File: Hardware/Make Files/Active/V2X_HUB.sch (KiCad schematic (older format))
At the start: 3 parts

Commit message: Saving V1.1 as archive.
We are trying a new architecture where the FTDI can be removed. making a
backup spot
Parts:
- removed F?: 1A, Resistors_SMD:R_1210, symbol FUSE
- removed P?: USB_A, Connect:USB_A, symbol USB_A
- removed P?: USB_u, Connect:USB_Micro-B, symbol USB_OTG
- added C58, C61: 1U, symbol C
- added C59, C60: 100N, symbol C
- added C62, C63: 18P, symbol C
- added R73, R77: DNS, symbol R
- added R74, R76, R78, R79: 1K0, symbol R
- added R75: 12K, symbol R
- added U18: USB2242, symbol USB2242
- added Y1: 24MHz, symbol Crystal_Small
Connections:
- net labels added: 3V3_B, FTDI_DM, FTDI_DP, HUB_CLK, HUB_CLKN, HUB_DM, HUB_DP, HUB_PWR_PRT1, HUB_PWR_PRT2, HUB_SCL, HUB_SDA, HUB_STATUS, HUB_SUSP, HUB_SUSP_IND, SIM_DM, SIM_DP, ~HUB_RESET
- net labels removed: 5V0, 5V0_OUT, USB_M, USB_P
- wire segments 3 -> 27
- no-connect marks 2 -> 3
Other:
- note added: "Boot Strapping Option\nPRTPWR1 = Battery Charge Enable\n0 = feature off, we dont need."
- note added: "Boot Strapping Option\nSUSP_IND = NON_REM0\nSMBDATA = NON_REM1\nNON_REM[1:0] = 10 \nmeans neither down port\n is removable \n\n\nSMBCLK = CFG_SEL = '0'\nMeans the hub is self powered"
- note added: "PRTPWR1 and PRTPWR2 go\n high when the port is active"
- note removed: "HOST Data/Power Connection"
- note removed: "HOST Power Connection"

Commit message: V1.2 mostly done
BOM is integrated and creates mouser orders
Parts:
- removed C58: 1U, symbol C
- removed C62, C63: 18P, symbol C
- removed R74, R76: 1K0, symbol R
- removed Y1: 24MHz, symbol Crystal_Small
- added C61: 100N, Capacitors_SMD:C_0603, symbol C
- added R80, R82: 1K0, symbol R
- added X?: 24MHz, symbol CRYSTAL_SMD
- C59: value 100N -> 1U; Mouse PN (none) -> 603-CC603KRX7R7BB105
- C60: footprint (none) -> Capacitors_SMD:C_0603; Mouse PN (none) -> 810-C1608X7R1E104K
- C62: renamed from C61; Mouse PN (none) -> 603-CC603KRX7R7BB105
- R78: Mouse PN (none) -> 71-CRCW0603-1.0K-E3
- R79: renamed from R75; Mouse PN (none) -> 71-CRCW0603-12K-E3
- R83: renamed from R79; Mouse PN (none) -> 71-CRCW0603-1.0K-E3
- U20: renamed from U18; Mouse PN (none) -> 579-USB2422/MJ
- renumbered R73 to R77, R77 to R81
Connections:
- net labels added: USB_INT_DM, USB_INT_DP
- net labels removed: FTDI_DM, FTDI_DP
- wire segments 27 -> 25

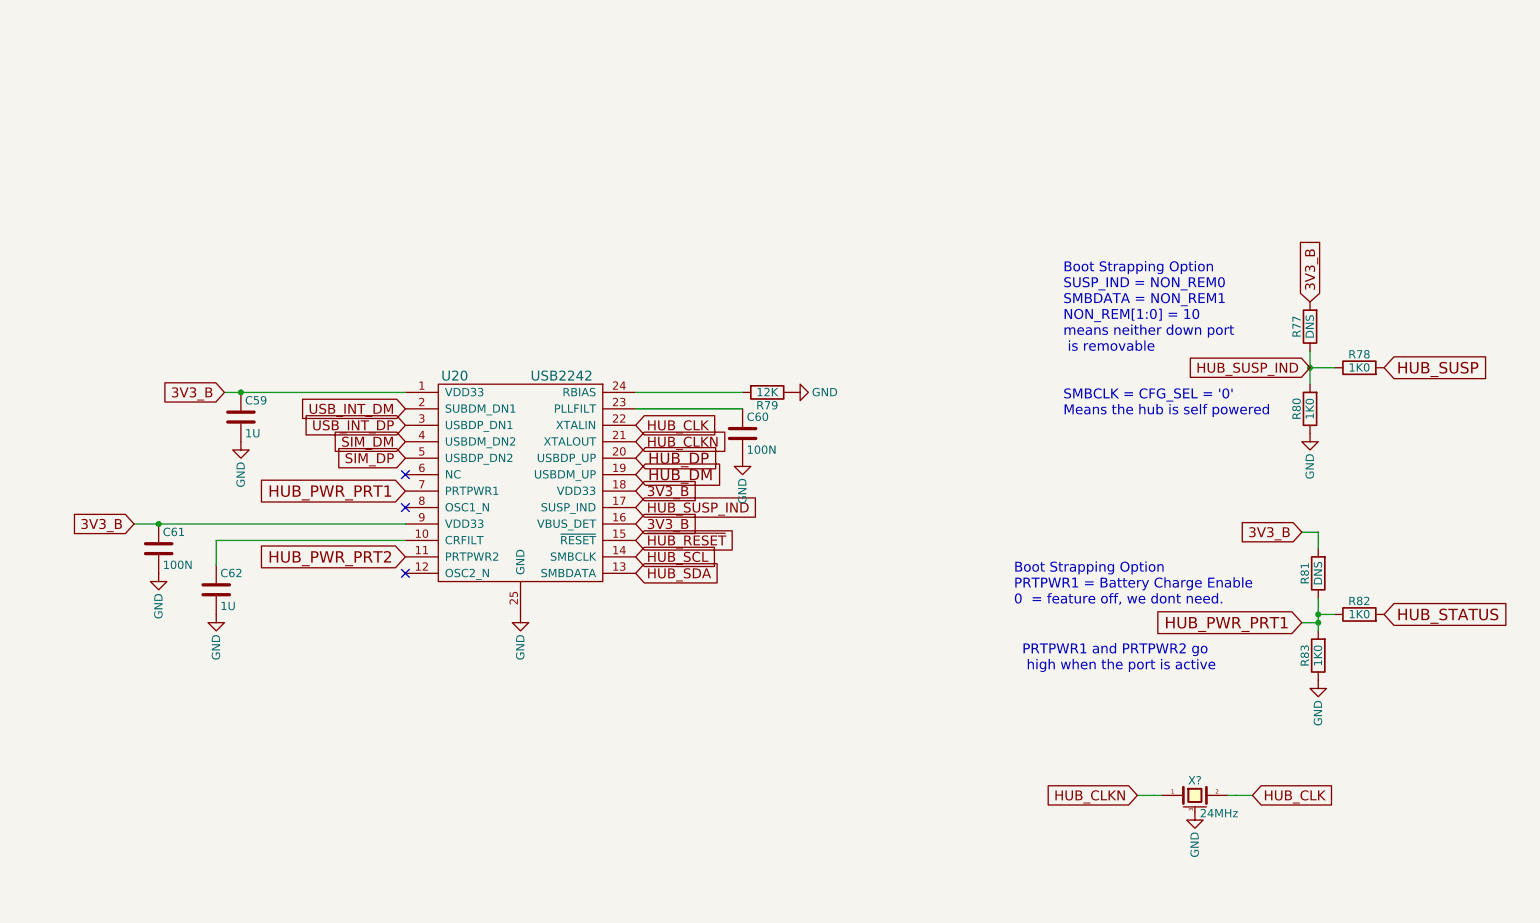
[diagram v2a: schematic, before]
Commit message: V2X v1.2 sch and bom
Made changes to the schematic to V1.2 (remove FTDI possibly) and
integrade the BOM information into the sch
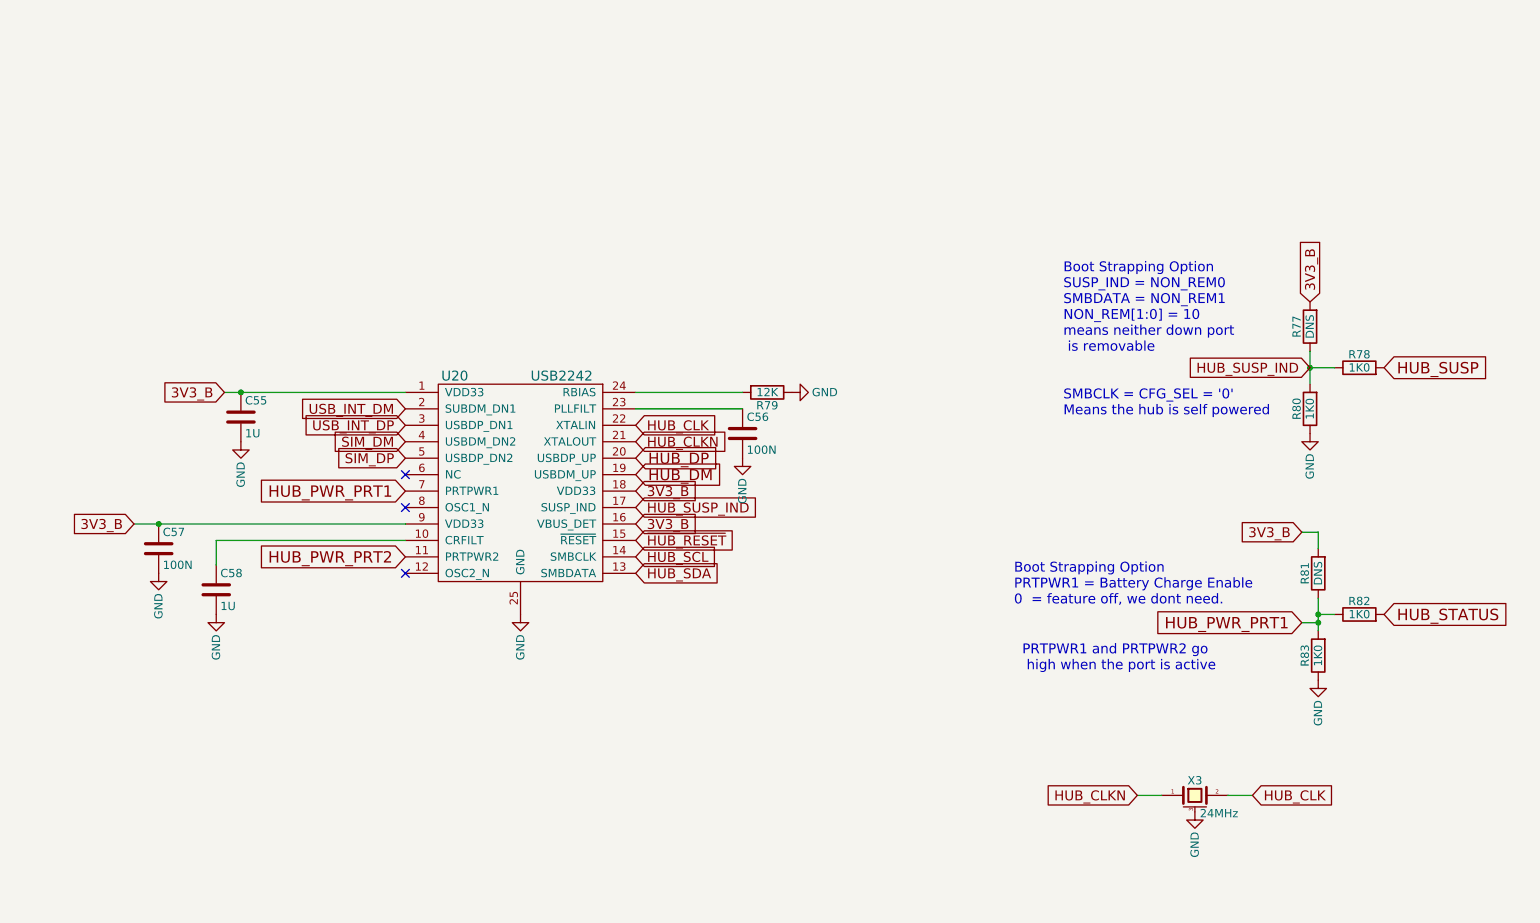
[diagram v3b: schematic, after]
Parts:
- gave numbers to parts that had none: 1
- renumbered C59 to C55, C60 to C56, C61 to C57, C62 to C58
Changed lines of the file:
@@
 3V3_B
 $Comp
-L GND #PWR0123
+L GND #PWR128
 U 1 1 55F890DF
 P 4350 4450
-F 0 "#PWR0123" H 4350 4200 50  0001 C CNN
+F 0 "#PWR128" H 4350 4200 50  0001 C CNN
 F 1 "GND" V 4350 4250 50  0000 C CNN
 F 2 "" H 4350 4450 60  0000 C CNN
@@
 HUB_CLKN
 Wire Wire Line
-	8100 5550 8200 5550
-Wire Wire Line
-	8200 5550 8250 5550
-Wire Wire Line
-	8650 5550 8700 5550
-Wire Wire Line
-	8700 5550 8800 5550
-$Comp
-L GND #PWR0124
+	8100 5550 8250 5550
+Wire Wire Line
+	8650 5550 8800 5550
+$Comp
+L GND #PWR130
 U 1 1 55F89454
 P 8450 5650
-F 0 "#PWR0124" H 8450 5400 50  0001 C CNN
+F 0 "#PWR130" H 8450 5400 50  0001 C CNN
 F 1 "GND" V 8450 5450 50  0000 C CNN
 F 2 "" H 8450 5650 60  0000 C CNN
@@
 $EndComp
 Wire Wire Line
-	9150 2850 9150 2950
-Wire Wire Line
-	9150 2950 9150 3050
+	9150 2850 9150 3050
 Connection ~ 9150 2950
 Text GLabel 9150 2550 1    60   Input ~ 0
@@
 $EndComp
 Wire Wire Line
-	9200 4350 9200 4450
-Wire Wire Line
-	9200 4450 9200 4500
-Wire Wire Line
-	9200 4500 9200 4550
+	9200 4350 9200 4550
 Connection ~ 9200 4450
 Text GLabel 9100 3950 0    60   Input ~ 0
 3V3_B
 $Comp
-L GND #PWR0126
+L GND #PWR129
 U 1 1 55F8A8AD
 P 9200 4850
-F 0 "#PWR0126" H 9200 4600 50  0001 C CNN
+F 0 "#PWR129" H 9200 4600 50  0001 C CNN
 F 1 "GND" V 9200 4650 50  0000 C CNN
 F 2 "" H 9200 4850 60  0000 C CNN
@@
 Boot Strapping Option\nPRTPWR1 = Battery Charge Enable\n0  = feature off, we dont need.
 $Comp
-L GND #PWR0127
+L GND #PWR122
 U 1 1 55F8AB65
 P 6000 3100
-F 0 "#PWR0127" H 6000 2850 50  0001 C CNN
+F 0 "#PWR122" H 6000 2850 50  0001 C CNN
 F 1 "GND" V 6000 2900 50  0000 C CNN
 F 2 "" H 6000 3100 60  0000 C CNN
@@
 	5700 3100 5050 3100
 Wire Wire Line
-	2000 3900 2150 3900
-Wire Wire Line
-	2150 3900 3650 3900
+	2000 3900 3650 3900
 Connection ~ 2150 3900
 $Comp
-L GND #PWR0128
+L GND #PWR126
 U 1 1 55F8AFDA
 P 2150 4200
-F 0 "#PWR0128" H 2150 3950 50  0001 C CNN
+F 0 "#PWR126" H 2150 3950 50  0001 C CNN
 F 1 "GND" V 2150 4000 50  0000 C CNN
 F 2 "" H 2150 4200 60  0000 C CNN
@@
 $EndComp
 Wire Wire Line
-	2550 3100 2650 3100
-Wire Wire Line
-	2650 3100 3650 3100
+	2550 3100 3650 3100
 Connection ~ 2650 3100
 $Comp
-L GND #PWR0129
+L GND #PWR124
 U 1 1 55F8B30B
 P 2650 3400
-F 0 "#PWR0129" H 2650 3150 50  0001 C CNN
+F 0 "#PWR124" H 2650 3150 50  0001 C CNN
 F 1 "GND" V 2650 3200 50  0000 C CNN
 F 2 "" H 2650 3400 60  0000 C CNN
@@
 $EndComp
 $Comp
-L C C62
+L C C58
 U 1 1 55F8B394
 P 2500 4300
-F 0 "C62" H 2525 4400 50  0000 L CNN
+F 0 "C58" H 2525 4400 50  0000 L CNN
 F 1 "1U" H 2525 4200 50  0000 L CNN
 F 2 "" H 2538 4150 30  0000 C CNN
@@
 	2500 4000 3650 4000
 $Comp
-L GND #PWR0130
+L GND #PWR127
 U 1 1 55F8B452
 P 2500 4450
-F 0 "#PWR0130" H 2500 4200 50  0001 C CNN
+F 0 "#PWR127" H 2500 4200 50  0001 C CNN
 F 1 "GND" V 2500 4250 50  0000 C CNN
 F 2 "" H 2500 4450 60  0000 C CNN
@@
 	5050 3200 5700 3200
 $Comp
-L GND #PWR0131
+L GND #PWR125
 U 1 1 55F8B6A0
 P 5700 3500
-F 0 "#PWR0131" H 5700 3250 50  0001 C CNN
+F 0 "#PWR125" H 5700 3250 50  0001 C CNN
 F 1 "GND" V 5700 3300 50  0000 C CNN
 F 2 "" H 5700 3500 60  0000 C CNN
@@
 HUB_SDA
 $Comp
-L GND #PWR0132
+L GND #PWR123
 U 1 1 55F9C2E3
 P 9150 3350
-F 0 "#PWR0132" H 9150 3100 50  0001 C CNN
+F 0 "#PWR123" H 9150 3100 50  0001 C CNN
 F 1 "GND" V 9150 3150 50  0000 C CNN
 F 2 "" H 9150 3350 60  0000 C CNN
@@
 HUB_PWR_PRT2
 $Comp
-L C C60
+L C C56
 U 1 1 56053852
 P 5700 3350
-F 0 "C60" H 5725 3450 50  0000 L CNN
+F 0 "C56" H 5725 3450 50  0000 L CNN
 F 1 "100N" H 5725 3250 50  0000 L CNN
 F 2 "Capacitors_SMD:C_0603" H 5738 3200 30  0001 C CNN
@@
 $EndComp
 $Comp
-L C C61
+L C C57
 U 1 1 56053914
 P 2150 4050
-F 0 "C61" H 2175 4150 50  0000 L CNN
+F 0 "C57" H 2175 4150 50  0000 L CNN
 F 1 "100N" H 2175 3950 50  0000 L CNN
 F 2 "Capacitors_SMD:C_0603" H 2188 3900 30  0001 C CNN
@@
 $EndComp
 $Comp
-L C C59
+L C C55
 U 1 1 56053A8A
 P 2650 3250
-F 0 "C59" H 2675 3350 50  0000 L CNN
+F 0 "C55" H 2675 3350 50  0000 L CNN
 F 1 "1U" H 2675 3150 50  0000 L CNN
 F 2 "" H 2688 3100 30  0000 C CNN
@@
 $EndComp
 $Comp
-L CRYSTAL_SMD X?
+L CRYSTAL_SMD X3
 U 1 1 56092E15
 P 8450 5550
-F 0 "X?" H 8450 5640 50  0000 C CNN
+F 0 "X3" H 8450 5640 50  0000 C CNN
 F 1 "24MHz" H 8480 5440 50  0000 L CNN
 F 2 "" H 8450 5550 60  0000 C CNN

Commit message: Split V2X in 2 boards, layout of SIM pcb done
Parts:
- C55, C58: footprint (none) -> Custom Parts:C_0603_SM
- C56, C57: footprint Capacitors_SMD:C_0603 -> Custom Parts:C_0603_SM
- R77, R78, R79, R80, R81, R82, R83: footprint (none) -> Custom Parts:R_0603_sm
- U20: footprint (none) -> Housings_DFN_QFN:QFN-24-1EP_4x4mm_Pitch0.5mm
- X3: footprint (none) -> Custom Parts:AWSCR
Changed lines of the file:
@@
 EESchema Schematic File Version 2
+LIBS:V2X-rescue
+LIBS:sim5320_KICAD_PART
+LIBS:CUSTOM_KICAD_PART
+LIBS:74xgxx
+LIBS:74xx
+LIBS:ac-dc
+LIBS:actel
+LIBS:adc-dac
+LIBS:Altera
+LIBS:analog_devices
+LIBS:analog_switches
+LIBS:atmel
+LIBS:audio
+LIBS:brooktre
+LIBS:cmos_ieee
+LIBS:cmos4000
+LIBS:conn
+LIBS:contrib
+LIBS:cypress
+LIBS:dc-dc
+LIBS:device
+LIBS:digital-audio
+LIBS:diode
+LIBS:display
+LIBS:dsp
+LIBS:elec-unifil
+LIBS:ESD_Protection
+LIBS:ftdi
+LIBS:gennum
+LIBS:graphic
+LIBS:hc11
+LIBS:intel
+LIBS:interface
+LIBS:ir
+LIBS:Lattice
+LIBS:linear
+LIBS:logo
+LIBS:maxim
+LIBS:memory
+LIBS:microchip
+LIBS:microchip_dspic33dsc
+LIBS:microchip_pic10mcu
+LIBS:microchip_pic12mcu
+LIBS:microchip_pic16mcu
+LIBS:microchip_pic18mcu
+LIBS:microchip_pic32mcu
+LIBS:microcontrollers
+LIBS:motor_drivers
+LIBS:motorola
+LIBS:msp430
+LIBS:nordicsemi
+LIBS:nxp_armmcu
+LIBS:onsemi
+LIBS:opto
+LIBS:Oscillators
+LIBS:philips
 LIBS:power
-LIBS:device
+LIBS:Power_Management
+LIBS:powerint
+LIBS:pspice
+LIBS:references
+LIBS:regul
+LIBS:relays
+LIBS:rfcom
+LIBS:sensors
+LIBS:silabs
+LIBS:siliconi
+LIBS:stm8
+LIBS:stm32
+LIBS:supertex
+LIBS:switches
+LIBS:texas
+LIBS:transf
 LIBS:transistors
-LIBS:conn
-LIBS:linear
-LIBS:regul
-LIBS:74xx
-LIBS:cmos4000
-LIBS:adc-dac
-LIBS:memory
+LIBS:ttl_ieee
+LIBS:valves
+LIBS:video
+LIBS:Xicor
 LIBS:xilinx
-LIBS:microcontrollers
-LIBS:dsp
-LIBS:microchip
-LIBS:analog_switches
-LIBS:motorola
-LIBS:texas
-LIBS:intel
-LIBS:audio
-LIBS:interface
-LIBS:digital-audio
-LIBS:philips
-LIBS:display
-LIBS:cypress
-LIBS:siliconi
-LIBS:opto
-LIBS:atmel
-LIBS:contrib
-LIBS:valves
-LIBS:sim5320_KICAD_PART
-LIBS:dc-dc
-LIBS:CUSTOM_KICAD_PART
+LIBS:Zilog
 LIBS:V2X-cache
 EELAYER 25 0
@@
 F 0 "U20" H 3950 4300 60  0000 C CNN
 F 1 "USB2242" H 4600 4300 60  0000 C CNN
-F 2 "" H 4350 3650 60  0000 C CNN
+F 2 "Housings_DFN_QFN:QFN-24-1EP_4x4mm_Pitch0.5mm" H 4350 3650 60  0001 C CNN
 F 3 "http://www.mouser.com/ds/2/268/2422-319423.pdf" H 4350 3650 60  0001 C CNN
 F 4 "579-USB2422/MJ" H 4350 3650 60  0001 C CNN "Mouse PN"
@@
 3V3_B
 $Comp
-L GND #PWR128
+L GND #PWR0131
 U 1 1 55F890DF
 P 4350 4450
-F 0 "#PWR128" H 4350 4200 50  0001 C CNN
+F 0 "#PWR0131" H 4350 4200 50  0001 C CNN
 F 1 "GND" V 4350 4250 50  0000 C CNN
 F 2 "" H 4350 4450 60  0000 C CNN
@@
 	8650 5550 8800 5550
 $Comp
-L GND #PWR130
+L GND #PWR0132
 U 1 1 55F89454
 P 8450 5650
-F 0 "#PWR130" H 8450 5400 50  0001 C CNN
+F 0 "#PWR0132" H 8450 5400 50  0001 C CNN
 F 1 "GND" V 8450 5450 50  0000 C CNN
 F 2 "" H 8450 5650 60  0000 C CNN
@@
 F 0 "R79" V 5930 3100 50  0000 C CNN
 F 1 "12K" V 5850 3100 50  0000 C CNN
-F 2 "" V 5780 3100 30  0000 C CNN
+F 2 "Custom Parts:R_0603_sm" V 5780 3100 30  0001 C CNN
 F 3 "http://www.mouser.com/ds/2/427/dcrcwe3-109170.pdf" H 5850 3100 30  0001 C CNN
 F 4 "71-CRCW0603-12K-E3" H 5850 3100 60  0001 C CNN "Mouse PN"
@@
 F 0 "R77" V 9230 2700 50  0000 C CNN
 F 1 "DNS" V 9150 2700 50  0000 C CNN
-F 2 "" V 9080 2700 30  0000 C CNN
+F 2 "Custom Parts:R_0603_sm" V 9080 2700 30  0001 C CNN
 F 3 "" H 9150 2700 30  0000 C CNN
 	1    9150 2700
@@
 F 0 "R81" V 9280 4200 50  0000 C CNN
 F 1 "DNS" V 9200 4200 50  0000 C CNN
-F 2 "" V 9130 4200 30  0000 C CNN
+F 2 "Custom Parts:R_0603_sm" V 9130 4200 30  0001 C CNN
 F 3 "" H 9200 4200 30  0000 C CNN
 	1    9200 4200
@@
 F 0 "R83" V 9280 4700 50  0000 C CNN
 F 1 "1K0" V 9200 4700 50  0000 C CNN
-F 2 "" V 9130 4700 30  0000 C CNN
+F 2 "Custom Parts:R_0603_sm" V 9130 4700 30  0001 C CNN
 F 3 "http://www.vishay.com/doc?20035" H 9200 4700 30  0001 C CNN
 F 4 "71-CRCW0603-1.0K-E3" H 9200 4700 60  0001 C CNN "Mouse PN"
@@
 3V3_B
 $Comp
-L GND #PWR129
+L GND #PWR0133
 U 1 1 55F8A8AD
 P 9200 4850
-F 0 "#PWR129" H 9200 4600 50  0001 C CNN
+F 0 "#PWR0133" H 9200 4600 50  0001 C CNN
 F 1 "GND" V 9200 4650 50  0000 C CNN
 F 2 "" H 9200 4850 60  0000 C CNN
@@
 Boot Strapping Option\nPRTPWR1 = Battery Charge Enable\n0  = feature off, we dont need.
 $Comp
-L GND #PWR122
+L GND #PWR0134
 U 1 1 55F8AB65
 P 6000 3100
-F 0 "#PWR122" H 6000 2850 50  0001 C CNN
+F 0 "#PWR0134" H 6000 2850 50  0001 C CNN
 F 1 "GND" V 6000 2900 50  0000 C CNN
 F 2 "" H 6000 3100 60  0000 C CNN
@@
 Connection ~ 2150 3900
 $Comp
-L GND #PWR126
+L GND #PWR0135
 U 1 1 55F8AFDA
 P 2150 4200
-F 0 "#PWR126" H 2150 3950 50  0001 C CNN
+F 0 "#PWR0135" H 2150 3950 50  0001 C CNN
 F 1 "GND" V 2150 4000 50  0000 C CNN
 F 2 "" H 2150 4200 60  0000 C CNN
@@
 Connection ~ 2650 3100
 $Comp
-L GND #PWR124
+L GND #PWR0136
 U 1 1 55F8B30B
 P 2650 3400
-F 0 "#PWR124" H 2650 3150 50  0001 C CNN
+F 0 "#PWR0136" H 2650 3150 50  0001 C CNN
 F 1 "GND" V 2650 3200 50  0000 C CNN
 F 2 "" H 2650 3400 60  0000 C CNN
@@
 F 0 "C58" H 2525 4400 50  0000 L CNN
 F 1 "1U" H 2525 4200 50  0000 L CNN
-F 2 "" H 2538 4150 30  0000 C CNN
+F 2 "Custom Parts:C_0603_SM" H 2538 4150 30  0001 C CNN
 F 3 "http://www.mouser.com/ds/2/447/UPY-GPHC_X7R_6.3V-to-50V_8-12304.pdf" H 2500 4300 60  0001 C CNN
 F 4 "603-CC603KRX7R7BB105" H 2500 4300 60  0001 C CNN "Mouse PN"
@@
 	2500 4000 3650 4000
 $Comp
-L GND #PWR127
+L GND #PWR0137
 U 1 1 55F8B452
 P 2500 4450
-F 0 "#PWR127" H 2500 4200 50  0001 C CNN
+F 0 "#PWR0137" H 2500 4200 50  0001 C CNN
 F 1 "GND" V 2500 4250 50  0000 C CNN
 F 2 "" H 2500 4450 60  0000 C CNN
@@
 	5050 3200 5700 3200
 $Comp
-L GND #PWR125
+L GND #PWR0138
 U 1 1 55F8B6A0
 P 5700 3500
-F 0 "#PWR125" H 5700 3250 50  0001 C CNN
+F 0 "#PWR0138" H 5700 3250 50  0001 C CNN
 F 1 "GND" V 5700 3300 50  0000 C CNN
 F 2 "" H 5700 3500 60  0000 C CNN
@@
 HUB_SDA
 $Comp
-L GND #PWR123
+L GND #PWR0139
 U 1 1 55F9C2E3
 P 9150 3350
-F 0 "#PWR123" H 9150 3100 50  0001 C CNN
+F 0 "#PWR0139" H 9150 3100 50  0001 C CNN
 F 1 "GND" V 9150 3150 50  0000 C CNN
 F 2 "" H 9150 3350 60  0000 C CNN
@@
 F 0 "C56" H 5725 3450 50  0000 L CNN
 F 1 "100N" H 5725 3250 50  0000 L CNN
-F 2 "Capacitors_SMD:C_0603" H 5738 3200 30  0001 C CNN
+F 2 "Custom Parts:C_0603_SM" H 5738 3200 30  0001 C CNN
 F 3 "http://www.mouser.com/ds/2/400/mlcc_commercial_general_en-266370.pdf" H 5700 3350 60  0001 C CNN
 F 4 "810-C1608X7R1E104K" H 5700 3350 60  0001 C CNN "Mouse PN"
@@
 F 0 "C57" H 2175 4150 50  0000 L CNN
 F 1 "100N" H 2175 3950 50  0000 L CNN
-F 2 "Capacitors_SMD:C_0603" H 2188 3900 30  0001 C CNN
+F 2 "Custom Parts:C_0603_SM" H 2188 3900 30  0001 C CNN
 F 3 "http://www.mouser.com/ds/2/400/mlcc_commercial_general_en-266370.pdf" H 2150 4050 60  0001 C CNN
 F 4 "810-C1608X7R1E104K" H 2150 4050 60  0001 C CNN "Mouse PN"
@@
 F 0 "C55" H 2675 3350 50  0000 L CNN
 F 1 "1U" H 2675 3150 50  0000 L CNN
-F 2 "" H 2688 3100 30  0000 C CNN
+F 2 "Custom Parts:C_0603_SM" H 2688 3100 30  0001 C CNN
 F 3 "http://www.mouser.com/ds/2/447/UPY-GPHC_X7R_6.3V-to-50V_8-12304.pdf" H 2650 3250 60  0001 C CNN
 F 4 "603-CC603KRX7R7BB105" H 2650 3250 60  0001 C CNN "Mouse PN"
@@
 F 0 "R80" V 9230 3200 50  0000 C CNN
 F 1 "1K0" V 9150 3200 50  0000 C CNN
-F 2 "" V 9080 3200 30  0000 C CNN
+F 2 "Custom Parts:R_0603_sm" V 9080 3200 30  0001 C CNN
 F 3 "http://www.vishay.com/doc?20035" H 9150 3200 30  0001 C CNN
 F 4 "71-CRCW0603-1.0K-E3" H 9150 3200 60  0001 C CNN "Mouse PN"
@@
 F 0 "R78" V 9530 2950 50  0000 C CNN
 F 1 "1K0" V 9450 2950 50  0000 C CNN
-F 2 "" V 9380 2950 30  0000 C CNN
+F 2 "Custom Parts:R_0603_sm" V 9380 2950 30  0001 C CNN
 F 3 "http://www.vishay.com/doc?20035" H 9450 2950 30  0001 C CNN
 F 4 "71-CRCW0603-1.0K-E3" H 9450 2950 60  0001 C CNN "Mouse PN"
@@
 F 0 "R82" V 9530 4450 50  0000 C CNN
 F 1 "1K0" V 9450 4450 50  0000 C CNN
-F 2 "" V 9380 4450 30  0000 C CNN
+F 2 "Custom Parts:R_0603_sm" V 9380 4450 30  0001 C CNN
 F 3 "http://www.vishay.com/doc?20035" H 9450 4450 30  0001 C CNN
 F 4 "71-CRCW0603-1.0K-E3" H 9450 4450 60  0001 C CNN "Mouse PN"
@@
 F 0 "X3" H 8450 5640 50  0000 C CNN
 F 1 "24MHz" H 8480 5440 50  0000 L CNN
-F 2 "" H 8450 5550 60  0000 C CNN
+F 2 "Custom Parts:AWSCR" H 8450 5550 60  0001 C CNN
 F 3 "http://www.abracon.com/Resonators/N_AWSCR-MT.pdf" H 8450 5550 60  0001 C CNN
 F 4 "815-AWSCR-24.00MTD-T" H 8450 5550 60  0001 C CNN "Mouse PN"
